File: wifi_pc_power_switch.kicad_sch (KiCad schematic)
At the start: 17 parts, among them J1 Conn_01x20_Socket, J2 Conn_01x20_Socket, J3 Conn_01x04_Socket, J4 Conn_01x03_Socket, J5 Conn_01x04_Socket, J6 Conn_01x04_Socket, J7 Conn_01x04_Socket, Q1 BSS123, U1 PicoW, U2 TLP175A

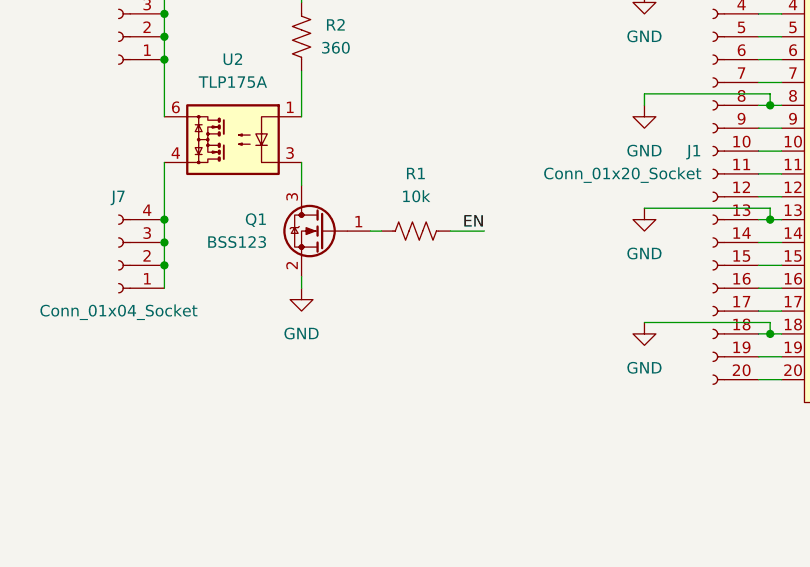
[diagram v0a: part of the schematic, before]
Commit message: Add pull-down to establish default switch state
 - Also force keep-out areas to be where they matter-- for USB and
   antenna, keep-out for both top and bottom layers. For test pads,
   keep-out only on top layer.
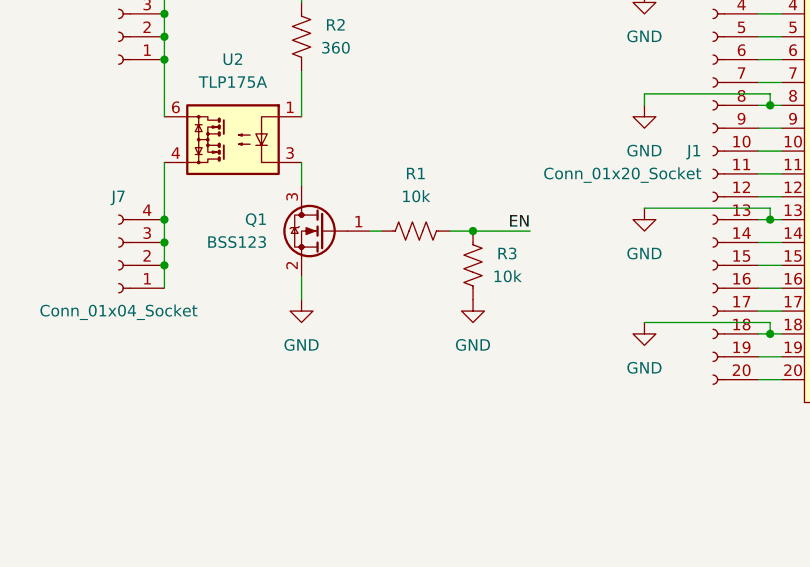
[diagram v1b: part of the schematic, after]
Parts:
- added R3: 10k, Resistor_SMD:R_0603_1608Metric_Pad0.98x0.95mm_HandSolder, symbol Device:R_US
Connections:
- net EN: now also R3.2
- net GND: now also R3.1
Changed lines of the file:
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@@
     (title "WiFi PC Power Switch")
     (date "2023-11-16")
-    (rev "A")
+    (rev "B")
     (comment 1 "Author: ${AUTHOR}")
   )
@@
   (junction (at 179.07 85.09) (diameter 0) (color 0 0 0 0)
   )
+  (junction (at 107.95 106.68) (diameter 0) (color 0 0 0 0)
+  )
   (junction (at 73.66 107.95) (diameter 0) (color 0 0 0 0)
   )
@@
     (stroke (width 0) (type default))
   )
-  (wire (pts (xy 105.41 106.68) (xy 109.22 106.68))
+  (wire (pts (xy 105.41 106.68) (xy 107.95 106.68))
     (stroke (width 0) (type default))
   )
@@
     (stroke (width 0) (type default))
   )
-  (wire (pts (xy 88.9 111.76) (xy 88.9 113.03))
+  (wire (pts (xy 88.9 111.76) (xy 88.9 114.3))
     (stroke (width 0) (type default))
   )
@@
   )
   (wire (pts (xy 22.86 177.8) (xy 34.29 177.8))
+    (stroke (width 0) (type default))
+  )
+  (wire (pts (xy 107.95 106.68) (xy 114.3 106.68))
     (stroke (width 0) (type default))
   )
@@
     (effects (font (size 1.27 1.27)) (justify right bottom))
   )
-  (label "EN" (at 109.22 106.68 180) (fields_autoplaced)
+  (label "EN" (at 114.3 106.68 180) (fields_autoplaced)
     (effects (font (size 1.27 1.27)) (justify right bottom))
   )
@@
     )
   )
-  (symbol (lib_id "power:GND") (at 88.9 113.03 0) (unit 1)
-    (in_bom yes) (on_board yes) (dnp no) (fields_autoplaced)
-    (property "Reference" "#PWR04" (at 88.9 119.38 0)
-      (effects (font (size 1.27 1.27)) hide)
-    )
-    (property "Value" "GND" (at 88.9 118.11 0)
-      (effects (font (size 1.27 1.27)))
-    )
-    (property "Footprint" "" (at 88.9 113.03 0)
-      (effects (font (size 1.27 1.27)) hide)
-    )
-    (property "Datasheet" "" (at 88.9 113.03 0)
+  (symbol (lib_id "power:GND") (at 88.9 114.3 0) (unit 1)
+    (in_bom yes) (on_board yes) (dnp no) (fields_autoplaced)
+    (property "Reference" "#PWR04" (at 88.9 120.65 0)
+      (effects (font (size 1.27 1.27)) hide)
+    )
+    (property "Value" "GND" (at 88.9 119.38 0)
+      (effects (font (size 1.27 1.27)))
+    )
+    (property "Footprint" "" (at 88.9 114.3 0)
+      (effects (font (size 1.27 1.27)) hide)
+    )
+    (property "Datasheet" "" (at 88.9 114.3 0)
       (effects (font (size 1.27 1.27)) hide)
     )
@@
         (path "/0ea637e9-b2c0-4dfc-b68d-b76c0fa2d617"
           (reference "#PWR02") (unit 1)
+        )
+      )
+    )
+  )
+  (symbol (lib_id "power:GND") (at 107.95 114.3 0) (unit 1)
+    (in_bom yes) (on_board yes) (dnp no) (fields_autoplaced)
+    (property "Reference" "#PWR012" (at 107.95 120.65 0)
+      (effects (font (size 1.27 1.27)) hide)
+    )
+    (property "Value" "GND" (at 107.95 119.38 0)
+      (effects (font (size 1.27 1.27)))
+    )
+    (property "Footprint" "" (at 107.95 114.3 0)
+      (effects (font (size 1.27 1.27)) hide)
+    )
+    (property "Datasheet" "" (at 107.95 114.3 0)
+      (effects (font (size 1.27 1.27)) hide)
+    )
+    (pin "1")
+    (instances
+      (project "wifi_pc_power_switch"
+        (path "/0ea637e9-b2c0-4dfc-b68d-b76c0fa2d617"
+          (reference "#PWR012") (unit 1)
         )
       )
@@
         )
       )
+    )
+  )
+  (symbol (lib_id "Device:R_US") (at 107.95 110.49 180) (unit 1)
+    (in_bom yes) (on_board yes) (dnp no)
+    (property "Reference" "R3" (at 111.76 109.22 0)
+      (effects (font (size 1.27 1.27)))
+    )
+    (property "Value" "10k" (at 111.76 111.76 0)
+      (effects (font (size 1.27 1.27)))
+    )
+    (property "Footprint" "Resistor_SMD:R_0603_1608Metric_Pad0.98x0.95mm_HandSolder" (at 106.934 110.236 90)
+      (effects (font (size 1.27 1.27)) hide)
+    )
+    (property "Datasheet" "~" (at 107.95 110.49 0)
+      (effects (font (size 1.27 1.27)) hide)
+    )
+    (property "Manufacturer Product Number" "" (at 107.95 110.49 0)
+      (effects (font (size 1.27 1.27)))
+    )
+    (property "Digikey Product Number" "" (at 107.95 110.49 0)
+      (effects (font (size 1.27 1.27)) hide)
+    )
+    (property "Mouser Product Number" "" (at 107.95 110.49 0)
+      (effects (font (size 1.27 1.27)) hide)
+    )
+    (pin "1")
+    (pin "2")
+    (instances
+      (project "wifi_pc_power_switch"
+        (path "/0ea637e9-b2c0-4dfc-b68d-b76c0fa2d617"
+          (reference "R3") (unit 1)
+        )
+      )

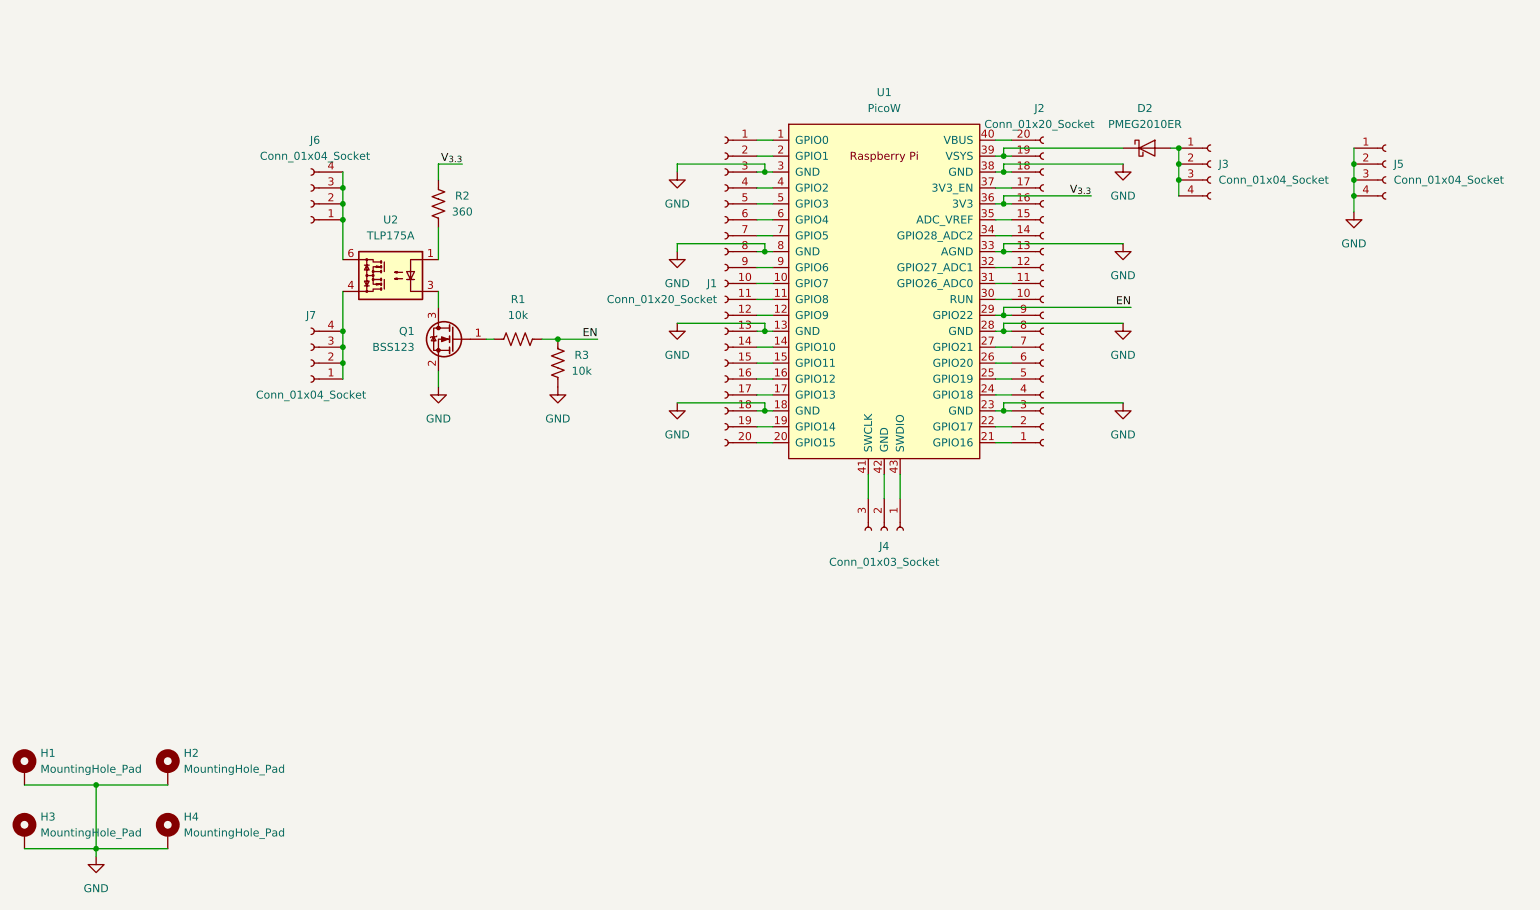
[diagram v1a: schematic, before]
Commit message: Revision B*: Tentative making everything denser
 - Added 5V notification LED, so it's easier to tell when the board is
   actually powered
 - Condensed the board appreciably
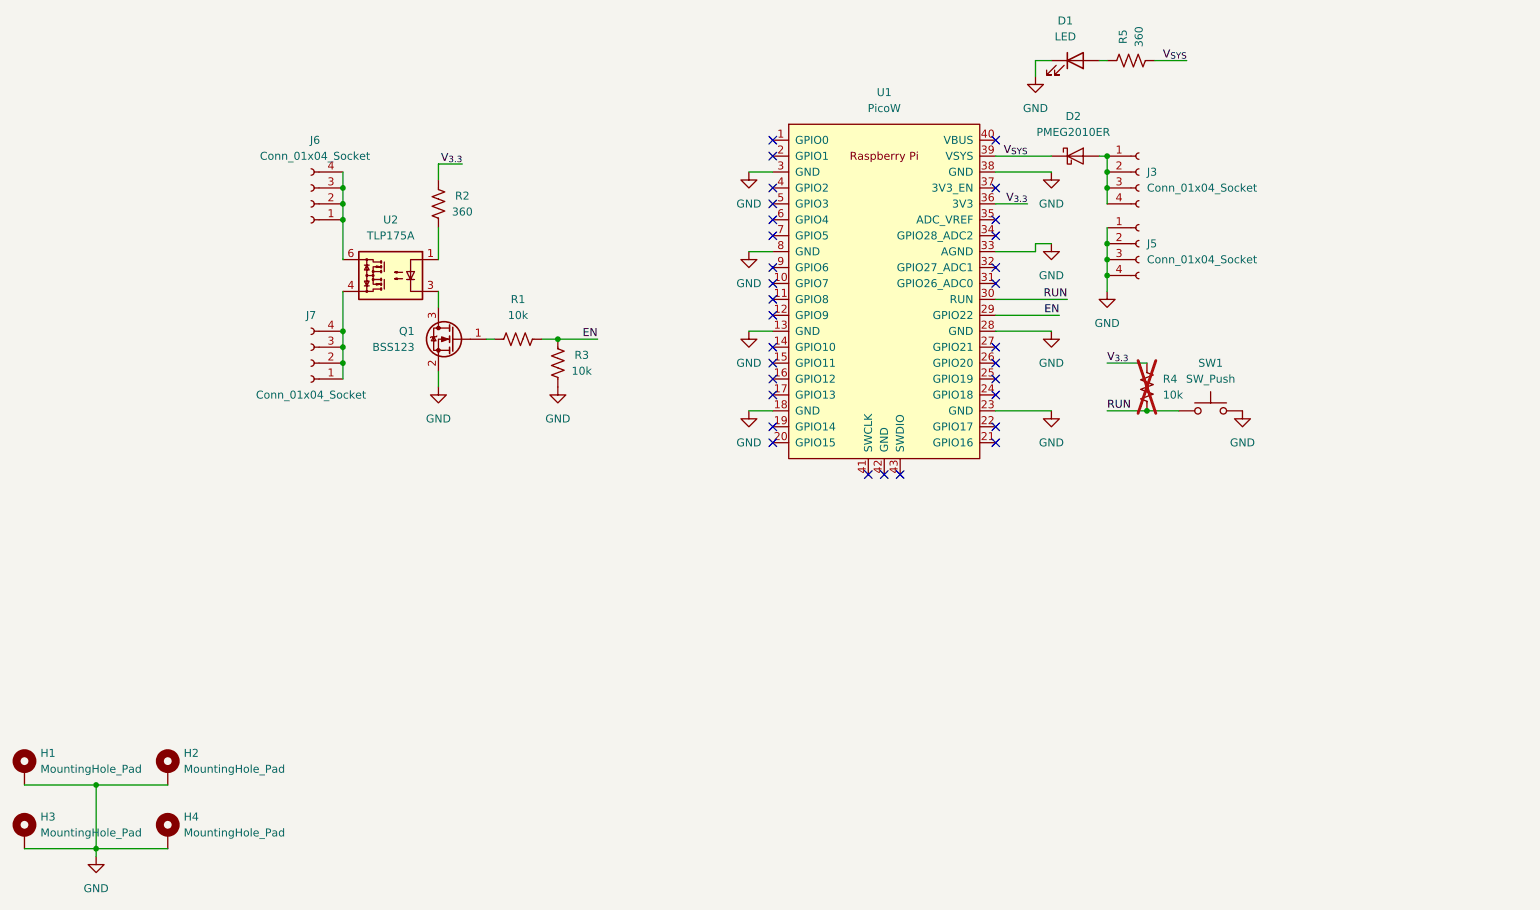
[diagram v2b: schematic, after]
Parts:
- removed J1, J2: Conn_01x20_Socket, Connector_PinSocket_2.54mm:PinSocket_1x20_P2.54mm_Vertical, symbol Connector:Conn_01x20_Socket
- removed J4: Conn_01x03_Socket, Connector_PinSocket_2.54mm:PinSocket_1x03_P2.54mm_Vertical, symbol Connector:Conn_01x03_Socket
- added D1: LED, LED_SMD:LED_0603_1608Metric_Pad1.05x0.95mm_HandSolder, symbol Device:LED
- added R4: 10k, Resistor_SMD:R_0603_1608Metric_Pad0.98x0.95mm_HandSolder, symbol Device:R_US
- added R5: 360, Resistor_SMD:R_0603_1608Metric_Pad0.98x0.95mm_HandSolder, symbol Device:R_US
- added SW1: SW_Push, Marcano:PTS636_SM50_SMTR_LFS, symbol Switch:SW_Push
- U1: footprint RPi_Pico:RPi_PicoW_SMD_TH -> RPi_PicoW:RPi_Pico_SMD_TH
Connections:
- net GND: now also D1.1 (K), SW1.2
- net V_{3.3}: now also R4.1
- net RUN: now reaches U1.30 (RUN)
- net RUN: now also R4.2, SW1.1
- net V_{SYS}: now reaches D2.1 (K), U1.39 (VSYS)
- net V_{SYS}: now also R5.1
- new net: D1.2 (A), R5.2
- no-connect marks 0 -> 31
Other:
- moved on the sheet: D2, J3, J5

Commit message: Add preliminary pico interface reboot support
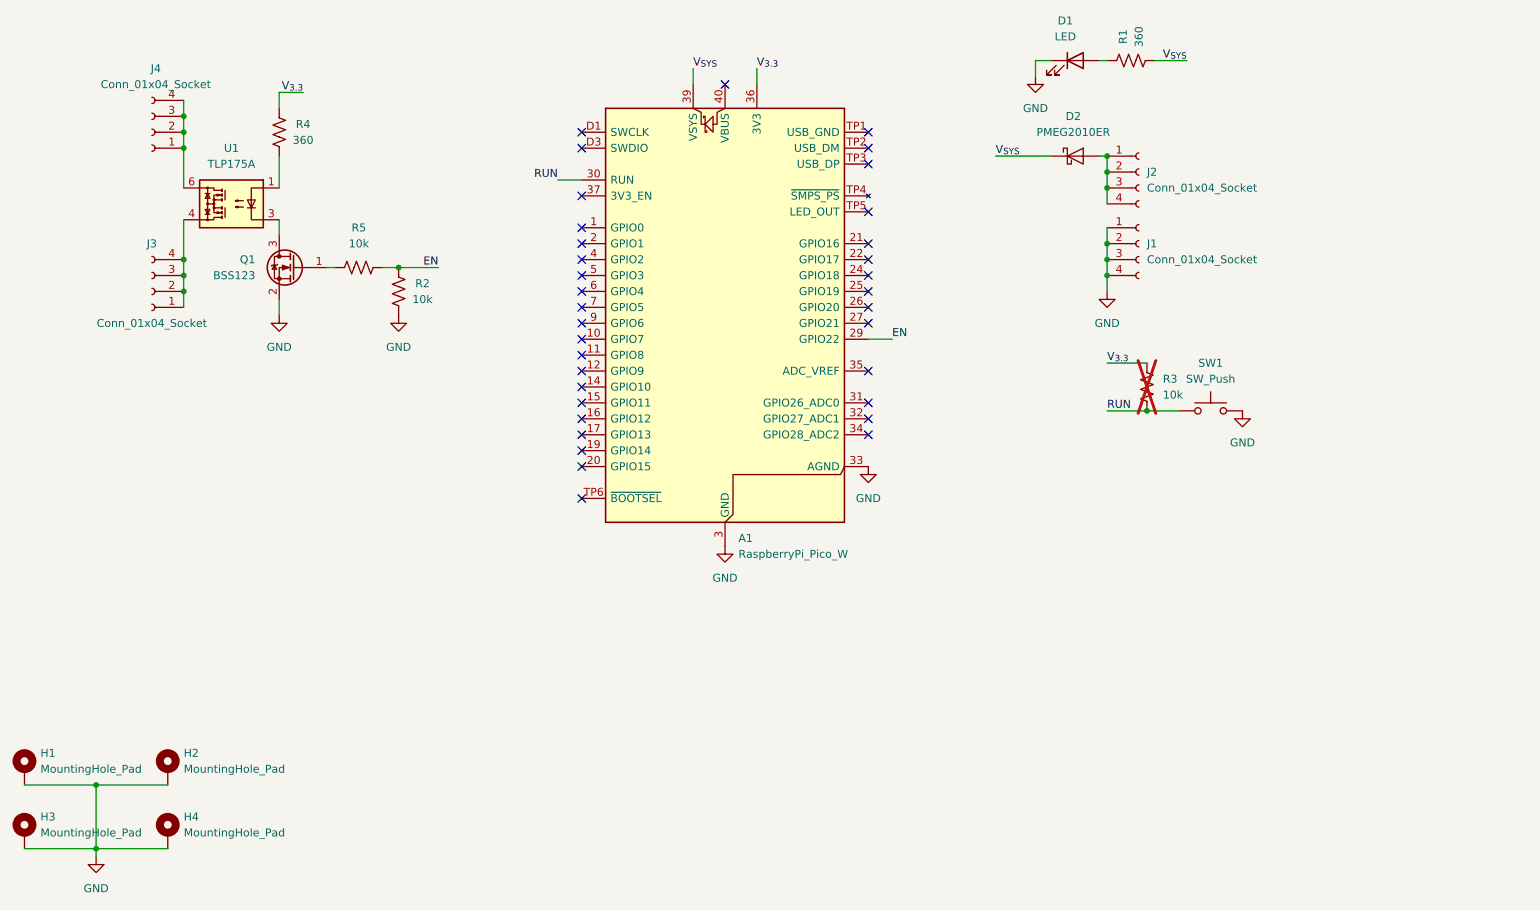
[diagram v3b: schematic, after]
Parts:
- removed U1: PicoW, RPi_PicoW:RPi_Pico_SMD_TH, symbol RPi_Pico:PicoW
- added A1: RaspberryPi_Pico_W, Marcano:RaspberryPi_Pico_W_Common_Unspecified, symbol MCU_Module:RaspberryPi_Pico_W_Extensive
- renumbered J5 to J1, J3 to J2, J7 to J3, J6 to J4, R5 to R1, R3 to R2, R4 to R3, R2 to R4, R1 to R5, U2 to U1
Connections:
- net EN: now also A1.29 (GPIO22)
- net GND: now also A1.13 (GND), A1.18 (GND), A1.23 (GND), A1.28 (GND), A1.3 (GND), A1.33 (AGND), A1.38 (GND), A1.8 (GND), A1.D2 (GND)
- net RUN: now also A1.30 (RUN)
- net V_{3.3}: now also A1.36 (3V3)
- net V_{SYS}: now also A1.39 (VSYS)
- no-connect marks 31 -> 35
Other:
- moved on the sheet: J3, J4, Q1, R2, R4, R5, U1

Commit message: We don't need that many pins, add sense
 - Reduce the 4x pins to 2x, and place them near the edge (to be used
   with simple screw terminals)
 - Add a sense line, so the MCU can tell if the computer is on. It needs
   a pulldown due to rp2350 E9 errata.
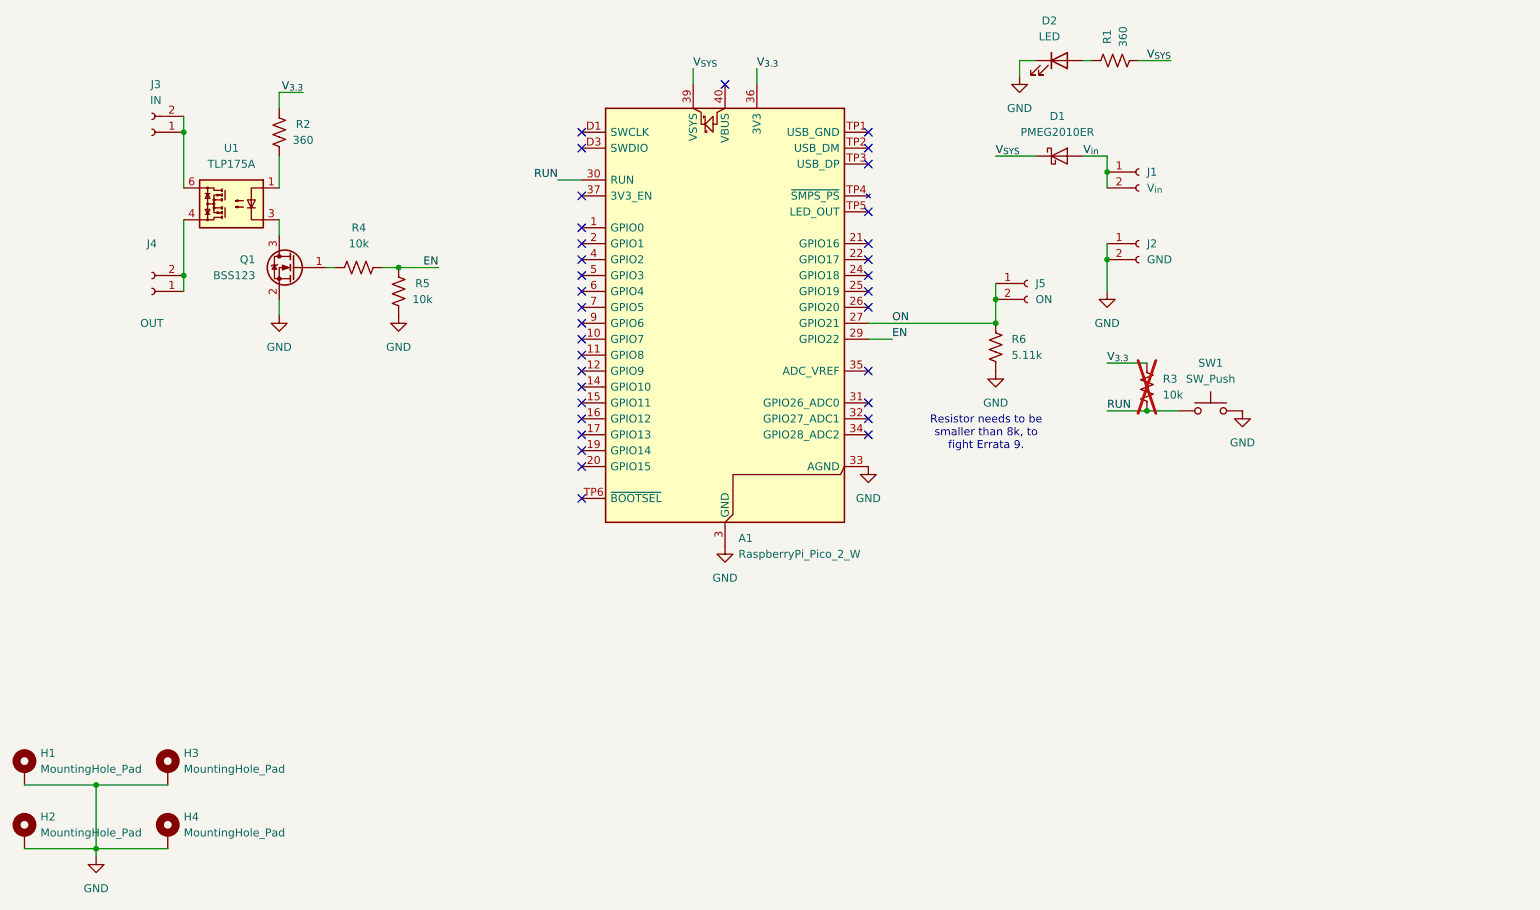
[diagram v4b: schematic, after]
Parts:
- added J5: ON, Connector_PinSocket_2.54mm:PinSocket_1x02_P2.54mm_Vertical, symbol Connector:Conn_01x02_Socket
- added R6: 5.11k, Capacitor_SMD:C_0603_1608Metric_Pad1.08x0.95mm_HandSolder, symbol Device:R_US
- A1: value RaspberryPi_Pico_W -> RaspberryPi_Pico_2_W; Digikey Product Number (none) -> 2648-SC1633CT-ND; Manufacturer Product Number (none) -> SC1633
- J1: renamed from J2; value Conn_01x04_Socket -> V_{in}; footprint Connector_PinSocket_2.54mm:PinSocket_1x04_P2.54mm_Vertical -> Connector_PinSocket_2.54mm:PinSocket_1x02_P2.54mm_Vertical; symbol Connector:Conn_01x04_Socket -> Connector:Conn_01x02_Socket
- J2: renamed from J1; value Conn_01x04_Socket -> GND; footprint Connector_PinSocket_2.54mm:PinSocket_1x04_P2.54mm_Vertical -> Connector_PinSocket_2.54mm:PinSocket_1x02_P2.54mm_Vertical; symbol Connector:Conn_01x04_Socket -> Connector:Conn_01x02_Socket
- J3: renamed from J4; value Conn_01x04_Socket -> IN; footprint Connector_PinSocket_2.54mm:PinSocket_1x04_P2.54mm_Vertical -> Connector_PinSocket_2.54mm:PinSocket_1x02_P2.54mm_Vertical; symbol Connector:Conn_01x04_Socket -> Connector:Conn_01x02_Socket
- J4: renamed from J3; value Conn_01x04_Socket -> OUT; footprint Connector_PinSocket_2.54mm:PinSocket_1x04_P2.54mm_Vertical -> Connector_PinSocket_2.54mm:PinSocket_1x02_P2.54mm_Vertical; symbol Connector:Conn_01x04_Socket -> Connector:Conn_01x02_Socket
- renumbered D2 to D1, D1 to D2, H3 to H2, H2 to H3, R4 to R2, R5 to R4, R2 to R5
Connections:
- net GND: now also R6.2; no longer J2.3 (Pin_3), J2.4 (Pin_4)
- net at J3.1 (Pin_1), J3.2 (Pin_2), U1.6: no longer J3.3 (Pin_3), J3.4 (Pin_4)
- net V_{in}: now reaches D1.2 (A), J1.1 (Pin_1), J1.2 (Pin_2)
- net V_{in}: no longer J1.3 (Pin_3), J1.4 (Pin_4)
- net ON: now reaches A1.27 (GPIO21)
- net ON: now also J5.1 (Pin_1), J5.2 (Pin_2), R6.1
- net at J4.1 (Pin_1), J4.2 (Pin_2), U1.4: no longer J4.3 (Pin_3), J4.4 (Pin_4)
- no-connect marks 35 -> 34
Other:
- note added: "Resistor needs to be smaller than 8k, to fight Errata 9."
- moved on the sheet: D1, D2, R1
